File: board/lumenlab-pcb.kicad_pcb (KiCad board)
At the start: 2 copper layers, 74 parts, among them J1 2.1mm Barrel Jack, J2 01x04, J3 01x06, J4 JTAG, SW1 SW_SPST, U1 MP2338, U2 AP7361C-33E, U3 SN74AHCT1G125, U4 SN74HC14DR, U5 ESP32-WROOM-32E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

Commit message: Separate pcb layout into separate modules
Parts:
- moved J4 442.1 mm to (-168.3, 343.3)
- moved C23 397.5 mm to (433.7, 279.1)
- moved R22 397.5 mm to (432.9, 285.0)
- moved RV1 381.6 mm to (455.4, 352.0)
- moved C5 374.8 mm to (253.0, -186.6)
- moved C6 374.8 mm to (258.0, -186.6)
- moved R4 374.8 mm to (247.0, -188.1)
- moved R8 374.8 mm to (247.0, -184.6)
- moved R21 363.5 mm to (337.1, 342.0)
- moved U1 352.9 mm to (212.2, -190.2)
- moved R9 346.3 mm to (453.0, 285.0)
- moved U7 343.1 mm to (450.0, 150.0)
- moved C7 336.2 mm to (368.6, -148.6)
- moved C8 336.2 mm to (373.8, -155.2)
- moved U2 336.2 mm to (342.9, -146.0)
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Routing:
- net +12V: track 0.63 -> 0.09 mm
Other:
- copper layers 2 -> 4

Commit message: Redesign the OLED user interface, implement USB programming
Due to testing with a hand soldered prototype, the original design of
using a five-way navigation tactile switch for the display navigation
was removed due to the button's fragility. A push button can be
registered as a push, down, and right command. The display will be
navigated using the PS3 controller, as that was already accessible.
USB-C periphials were added for more universal firmware updates, instead
of requiring the use of the ESP-Prog.
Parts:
- removed C24: 0.1uF, Capacitor_SMD:C_0603_1608Metric_Pad1.08x0.95mm_HandSolder
- removed R18: 100, Resistor_SMD:R_0603_1608Metric_Pad0.98x0.95mm_HandSolder
- removed R19, R22: 47K, Resistor_SMD:R_0603_1608Metric_Pad0.98x0.95mm_HandSolder
- removed S1: JS5208, 2_Vendor_NavSwitch:504-nav-switch
- removed U4: SN74HC14DR, 2_Vendor_SN74HC14N:sn74hc14dr
- added D2: ESD122DMYR, 2_Vendor_ESD122:DIO_ESD122DMYR, F.Cu at (-124.1, 136.7)
- added J5: USB_C_Receptacle_USB2.0_16P, Connector_USB:USB_C_Receptacle_JAE_DX07S016JA1R1500, F.Cu at (-154.7, 132.7)
- added U8: CP2102N-Axx-xQFN24, Package_DFN_QFN:QFN-24-1EP_4x4mm_P0.5mm_EP2.15x2.15mm, F.Cu at (-157.5, 140.5)
- C19, C20: value 0.1uF -> 100nF
- R12, R9: value 47K -> 5.1K
- R13, R14: value 100 -> 1K
- R15: value 100 -> 10K
- R16: value 47K -> 22
- R17: value 100 -> 22
- SW1: moved to B.Cu
- moved R16 634.2 mm to (-128.1, 136.5)
- moved R17 597.7 mm to (-128.1, 142.0)
- moved SW1 302.8 mm to (251.9, 100.0), turned to 180 degrees
- moved J1 298.2 mm to (252.9, 60.0), turned to 90 degrees
- moved C2 287.5 mm to (213.5, 90.0)
- moved C5 287.5 mm to (179.6, 91.4)
- moved C6 287.5 mm to (184.6, 91.4)
- moved R4 287.5 mm to (173.6, 89.9)
- moved R8 287.5 mm to (173.6, 93.4)
- moved U1 287.5 mm to (138.8, 87.8)
- moved C1 273.6 mm to (142.9, 101.5)
- moved C10 273.6 mm to (185.3, 105.3)
- moved C3 273.6 mm to (193.5, 105.5)
- moved C9 273.6 mm to (186.3, 114.9)
- moved L1 273.6 mm to (176.3, 110.5)
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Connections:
- C15 pad 1: /DEBOUNCE_UP -> +3.3V
- C18 pad 1: GND -> +3.3V
- C18 pad 2: +3.3V -> GND
- C19 pad 1: /DEBOUNCE_DOWN -> Net-(U8-~{DTR})
- C19 pad 2: GND -> /ESP32_GPIO0
- C20 pad 1: /DEBOUNCE_LEFT -> Net-(U8-~{RTS})
- C20 pad 2: GND -> /ESP32_EN
- C23 pad 1: /DEBOUNCE_RIGHT -> Net-(U8-~{RST})
- R10 pad 2: Net-(U5-EN) -> /ESP32_EN
- R11 pad 2: Net-(U5-IO0) -> /ESP32_GPIO0
- R12 pad 1: +3.3V -> Net-(J5-CC2)
- R12 pad 2: /DEBOUNCE_DOWN -> GND
- R13 pad 1: /ESP32_GPIO32 -> Net-(U8-RXD)
- R13 pad 2: Net-(U4-1Y) -> /ESP32_TX
- R14 pad 1: /ESP32_GPIO27 -> Net-(U8-TXD)
- R14 pad 2: Net-(U4-5Y) -> /ESP32_RX
- R15 pad 1: /ESP32_GPIO33 -> Net-(U8-~{RST})
- R15 pad 2: Net-(U4-2Y) -> +3.3V
- R16 pad 1: +3.3V -> Net-(D2-Pad2)
- R16 pad 2: /DEBOUNCE_LEFT -> /DATA-
- R17 pad 2: /ESP32_GPIO35 -> /DATA+
- R9 pad 1: +3.3V -> Net-(J5-CC1)
- R9 pad 2: /DEBOUNCE_UP -> GND
- TP1 pad 1: Net-(U5-EN) -> /ESP32_EN
- TP2 pad 1: Net-(U5-IO0) -> /ESP32_GPIO0
- U5 pad 12: /ESP32_GPIO27 -> unconnected-(U5-IO27-Pad12)
- U5 pad 25: Net-(U5-IO0) -> /ESP32_GPIO0
- U5 pad 3: Net-(U5-EN) -> /ESP32_EN
- U5 pad 31: /ESP32_GPIO19 -> unconnected-(U5-IO19-Pad31)
- U5 pad 34: unconnected-(U5-RXD0/IO3-Pad34) -> /ESP32_RX
- U5 pad 35: unconnected-(U5-TXD0/IO1-Pad35) -> /ESP32_TX
- U5 pad 7: /ESP32_GPIO35 -> unconnected-(U5-IO35-Pad7)
- U5 pad 8: /ESP32_GPIO32 -> unconnected-(U5-IO32-Pad8)
- U5 pad 9: /ESP32_GPIO33 -> unconnected-(U5-IO33-Pad9)
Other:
- board outline added: 195 x 111 mm

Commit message: Replace LED strip bare THT pads with JST 3.96mm. Replace decoupling THT cap for SMD
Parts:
- removed R20: 10, Resistor_SMD:R_0603_1608Metric_Pad0.98x0.95mm_HandSolder
- removed R21: 1K, Resistor_SMD:R_0603_1608Metric_Pad0.98x0.95mm_HandSolder
- removed U8: CP2102N-Axx-xQFN24, Package_DFN_QFN:QFN-24-1EP_4x4mm_P0.5mm_EP2.15x2.15mm
- added R18: 22, Resistor_SMD:R_0603_1608Metric_Pad0.98x0.95mm_HandSolder, F.Cu at (34.1, 322.5)
- added R19: 22, Resistor_SMD:R_0603_1608Metric_Pad0.98x0.95mm_HandSolder, F.Cu at (34.1, 325.0)
- added U4: SSD1306, 2_Custom_SSD1306:SSD1306_OLED_MODULE, F.Cu at (18.1, 335.4)
- C13: footprint 2_Vendor_16SEPF:CAPPRD500W60D1000H1300 -> 2_Vendor_EMZS250ARA102:CAP_JA0_NIP
- C16: value 0.1uF -> 1000uF; footprint Capacitor_SMD:C_0603_1608Metric_Pad1.08x0.95mm_HandSolder -> 2_Vendor_EMZS250ARA102:CAP_JA0_NIP
- C17: value 1000uF -> 0.1uF; footprint 2_Vendor_16SEPF:CAPPRD500W60D1000H1300 -> Capacitor_SMD:C_0603_1608Metric_Pad1.08x0.95mm_HandSolder
- C19: value 100nF -> 0.1uF
- C20: value 100nF -> 250uF; footprint Capacitor_SMD:C_0603_1608Metric_Pad1.08x0.95mm_HandSolder -> 2_Vendor_10TZV220M6:CAP_J-V_6P3X8_RUB-M
- C21: value 250uF -> 0.05uF; footprint 2_Vendor_10TZV220M6:CAP_J-V_6P3X8_RUB-M -> Capacitor_SMD:C_1206_3216Metric_Pad1.33x1.80mm_HandSolder
- C22: value 0.05uF -> 0.1uF; footprint Capacitor_SMD:C_1206_3216Metric_Pad1.33x1.80mm_HandSolder -> Capacitor_SMD:C_0603_1608Metric_Pad1.08x0.95mm_HandSolder
- J2: value 01x04 -> 01x06; footprint Connector_Wire:SolderWire-0.75sqmm_1x04_P7mm_D1.25mm_OD3.5mm -> Connector_JST:JST_VH_B6PS-VH_1x06_P3.96mm_Horizontal
- J3: value 01x06 -> 01x04; footprint Connector_Wire:SolderWire-0.75sqmm_1x06_P7mm_D1.25mm_OD3.5mm -> Connector_JST:JST_VH_B4PS-VH_1x04_P3.96mm_Horizontal
- R11, R15: value 10K -> 1K
- R12, R9: value 5.1K -> 10K
- R14: value 1K -> 10
- R16, R17: value 22 -> 5.1K
- R5: value 10K -> 330
- R6: value 330 -> 10K
- U5: value ESP32-WROOM-32E -> LM386MX; footprint RF_Module:ESP32-WROOM-32E -> digikey-footprints:SOIC-8_W3.9mm
- U6: value LM386MX -> ESP32-WROOM-32E; footprint digikey-footprints:SOIC-8_W3.9mm -> RF_Module:ESP32-WROOM-32E
- U7: value SSD1306 -> CP2102N-Axx-xQFN24; footprint 2_Custom_SSD1306:SSD1306_OLED_MODULE -> Package_DFN_QFN:QFN-24-1EP_4x4mm_P0.5mm_EP2.15x2.15mm
- moved H1 429.5 mm to (259.0, 51.0)
- moved F1 15.9 mm to (251.9, 67.8)
- moved C16 15.0 mm to (160.5, 362.0)
- moved D1 8.93 mm to (248.0, 60.0), turned to -90 degrees
- moved C13 7.16 mm to (139.0, 362.0)
- moved C14 7.00 mm to (185.0, 342.2)
- moved J2 6.46 mm to (154.1, 329.2)
- moved J1 6.13 mm to (259.0, 61.0)
- moved C17 6.12 mm to (176.1, 360.0)
- moved SW1 2.30 mm to (254.0, 99.0)
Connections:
- C15 pad 1: +3.3V -> +12V
- C17 pad 1: +12V -> +3.3V
- C19 pad 1: Net-(U8-~{DTR}) -> Net-(U7-~{RST})
- C19 pad 2: /ESP32_GPIO0 -> GND
- C20 pad 1: Net-(U8-~{RTS}) -> Net-(C20-Pad1)
- C20 pad 2: /ESP32_EN -> Net-(C20-Pad2)
- C21 pad 1: Net-(C21-Pad1) -> Net-(C20-Pad1)
- C22 pad 1: Net-(C21-Pad1) -> Net-(U7-~{RTS})
- C22 pad 2: Net-(C22-Pad2) -> /ESP32_EN
- C23 pad 1: Net-(U8-~{RST}) -> Net-(U7-~{DTR})
- C23 pad 2: GND -> /ESP32_GPIO0
- J2 pad 3: GND -> /LED_DIN
- J2 pad 4: GND -> /LED_DIN
- J3 pad 3: /LED_DIN -> GND
- J3 pad 4: /LED_DIN -> GND
- LS1 pad 1: Net-(C21-Pad2) -> Net-(C20-Pad2)
- R10 pad 2: /ESP32_EN -> /ESP32_GPIO0
- R11 pad 1: +3.3V -> Net-(U7-TXD)
- R11 pad 2: /ESP32_GPIO0 -> /ESP32_RX
- R12 pad 1: Net-(J5-CC2) -> Net-(U7-~{RST})
- R12 pad 2: GND -> +3.3V
- R13 pad 1: Net-(U8-RXD) -> Net-(U7-RXD)
- R14 pad 1: Net-(U8-TXD) -> GND
- R14 pad 2: /ESP32_RX -> Net-(C21-Pad2)
- R15 pad 1: Net-(U8-~{RST}) -> Net-(R15-Pad1)
- R15 pad 2: +3.3V -> /ESP32_GPIO34
- R16 pad 1: Net-(D2-Pad2) -> Net-(J5-CC1)
- R16 pad 2: /DATA- -> GND
- R17 pad 1: Net-(D2-Pad3) -> Net-(J5-CC2)
- R17 pad 2: /DATA+ -> GND
- R5 pad 1: /BUCK_PG -> Net-(U3-Y)
- R5 pad 2: +5V -> /LED_DIN
- R6 pad 1: Net-(U3-Y) -> /BUCK_PG
- R6 pad 2: /LED_DIN -> +5V
- R9 pad 1: Net-(J5-CC1) -> +3.3V
- R9 pad 2: GND -> /ESP32_EN
- RV2 pad 2: Net-(R21-Pad1) -> Net-(R15-Pad1)
- U5 pad 1: GND -> unconnected-(U5-Pad1)
- U5 pad 2: +3.3V -> GND
- U5 pad 3: /ESP32_EN -> /AMP_IN
- U5 pad 4: unconnected-(U5-SENSOR_VP-Pad4) -> GND
- U5 pad 5: unconnected-(U5-SENSOR_VN-Pad5) -> Net-(C20-Pad1)
- U5 pad 6: /ESP32_GPIO34 -> +5V
- U6 pad 1: unconnected-(U6-Pad1) -> GND
- U6 pad 2: GND -> +3.3V
- U6 pad 3: /AMP_IN -> /ESP32_EN
- U6 pad 4: GND -> unconnected-(U6-SENSOR_VP-Pad4)
- U6 pad 5: Net-(C21-Pad1) -> unconnected-(U6-SENSOR_VN-Pad5)
- U6 pad 6: +5V -> /ESP32_GPIO34
- U7 pad 1: GND -> unconnected-(U7-~{RI}/CLK-Pad1)
- U7 pad 2: +5V -> GND
- U7 pad 3: /ESP32_GPIO22 -> /DATA+
- U7 pad 4: /ESP32_GPIO21 -> /DATA-

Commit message: Place power delivery, power protection, and step-down regulator
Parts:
- moved C7 363.7 mm to (125.6, 122.0)
- moved C8 363.7 mm to (130.7, 115.3)
- moved H2 361.0 mm to (235.0, 137.0)
- moved U2 352.4 mm to (127.2, 132.7)
- moved C22 316.9 mm to (503.1, 154.0)
- moved U6 264.7 mm to (168.2, 75.6), turned to 0 degrees
- moved J3 241.9 mm to (227.2, 107.9), turned to 90 degrees
- moved R6 239.7 mm to (214.0, 129.0), turned to -90 degrees
- moved C21 235.2 mm to (483.6, 268.0)
- moved R5 222.4 mm to (351.9, -46.0)
- moved LS1 160.0 mm to (383.0, 345.4)
- moved U1 83.0 mm to (213.0, 124.8), turned to 180 degrees
- moved C1 72.9 mm to (209.2, 131.8), turned to 180 degrees
- moved R2 72.4 mm to (212.0, 129.0), turned to -90 degrees
- moved R3 68.8 mm to (209.1, 128.8), turned to 180 degrees
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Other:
- board size 195 x 111 mm -> 148.5 x 80 mm

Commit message: Add LDO, signal JST connector, OLED display, and UI potentiometers
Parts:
- added TP6: LED_SIG, TestPoint:TestPoint_THTPad_D2.0mm_Drill1.0mm, F.Cu at (-158.0, 255.0)
- RV1, RV2: footprint Potentiometer_THT:Potentiometer_Piher_T-16L_Single_Vertical_Hole -> 2_Custom_Potentiometer:Potentiometer; moved to F.Cu
- TP1: value TestPoint -> 12V
- TP2: value TestPoint -> EN
- TP3: value TestPoint -> IO0
- TP4: value TestPoint -> 3.3V
- TP5: value TestPoint -> 5V
- U4: moved to B.Cu
- moved TP1 678.6 mm to (-158.0, 223.0)
- moved TP2 601.0 mm to (-158.0, 232.0)
- moved RV1 403.7 mm to (127.5, 116.5), turned to -90 degrees
- moved R12 375.0 mm to (176.5, 72.7), turned to -90 degrees
- moved R9 372.4 mm to (138.9, 85.0)
- moved C22 370.2 mm to (139.0, 87.5)
- moved C19 364.0 mm to (179.4, 71.8)
- moved C11 360.7 mm to (133.4, 80.0)
- moved C12 355.1 mm to (138.9, 82.0)
- moved J5 354.6 mm to (196.3, 82.5), turned to 90 degrees
- moved R15 346.6 mm to (132.5, 114.2)
- moved TP4 339.8 mm to (139.0, 79.0)
- moved C15 337.5 mm to (187.0, 119.1), turned to 90 degrees
- moved H3 327.5 mm to (103.0, 73.0)
- moved R13 327.1 mm to (165.1, 81.5), turned to 180 degrees
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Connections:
- TP1 pad 1: /ESP32_EN -> +12V
- TP2 pad 1: /ESP32_GPIO0 -> /ESP32_EN
- TP3 pad 1: +3.3V -> /ESP32_GPIO0
- TP4 pad 1: +5V -> +3.3V
- TP5 pad 1: /LED_DIN -> +5V
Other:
- board size 148.5 x 80 mm -> 100 x 65 mm
- copper layers 4 -> 2

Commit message: Place remaining components, audo, JTAG, filters
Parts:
- added C24: 0.1uF, Capacitor_SMD:C_0603_1608Metric_Pad1.08x0.95mm_HandSolder, F.Cu at (164.1, 95.5)
- added R20: 4.7K, Resistor_SMD:R_0603_1608Metric_Pad0.98x0.95mm_HandSolder, F.Cu at (164.1, 84.5)
- added R21: 4.7K, Resistor_SMD:R_0603_1608Metric_Pad0.98x0.95mm_HandSolder, F.Cu at (164.1, 80.0)
- R7: value 100 -> 33
- moved J4 402.2 mm to (152.2, 100.2)
- moved C21 357.8 mm to (120.0, 106.8)
- moved R14 357.8 mm to (120.0, 109.0)
- moved TP1 356.2 mm to (184.9, 126.6)
- moved C20 353.1 mm to (119.0, 121.8), turned to -90 degrees
- moved TP3 352.8 mm to (165.5, 99.2)
- moved U5 340.9 mm to (118.3, 101.3), turned to 90 degrees
- moved LS1 329.5 mm to (119.0, 129.9)
- moved TP2 329.4 mm to (143.5, 99.2)
- moved TP5 316.3 mm to (110.5, 81.0)
- moved TP6 308.6 mm to (116.5, 114.0)
- moved R5 281.5 mm to (120.2, 114.0), turned to 180 degrees
- moved R7 264.8 mm to (164.1, 89.0), turned to 180 degrees
- moved C4 261.2 mm to (164.1, 94.0), turned to 180 degrees
- moved U3 236.1 mm to (164.6, 91.5), turned to 180 degrees
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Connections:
- U4 pad 3: /ESP32_GPIO22 -> Net-(U4-SCL)
- U4 pad 4: /ESP32_GPIO21 -> Net-(U4-SDA)
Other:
- outline, holes or cut-outs redrawn

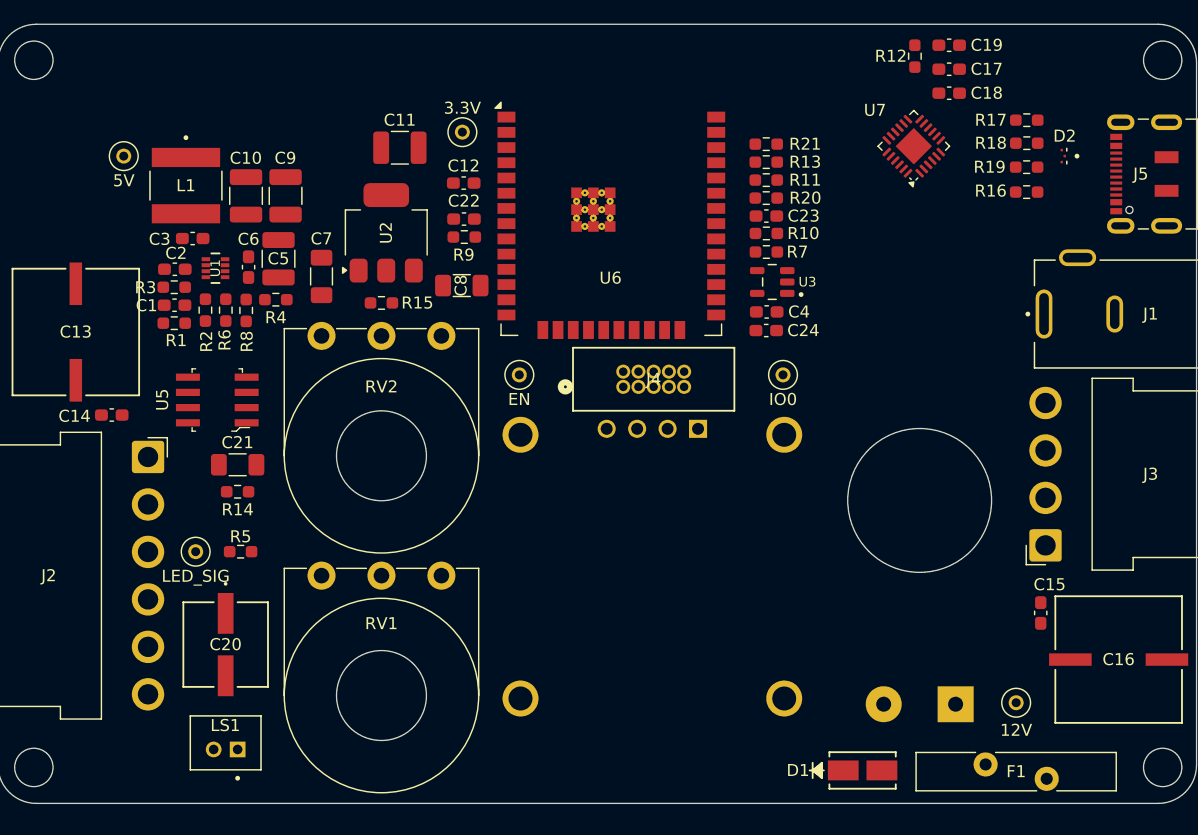
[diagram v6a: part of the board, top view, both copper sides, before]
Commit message: Route traces, tune differential pair
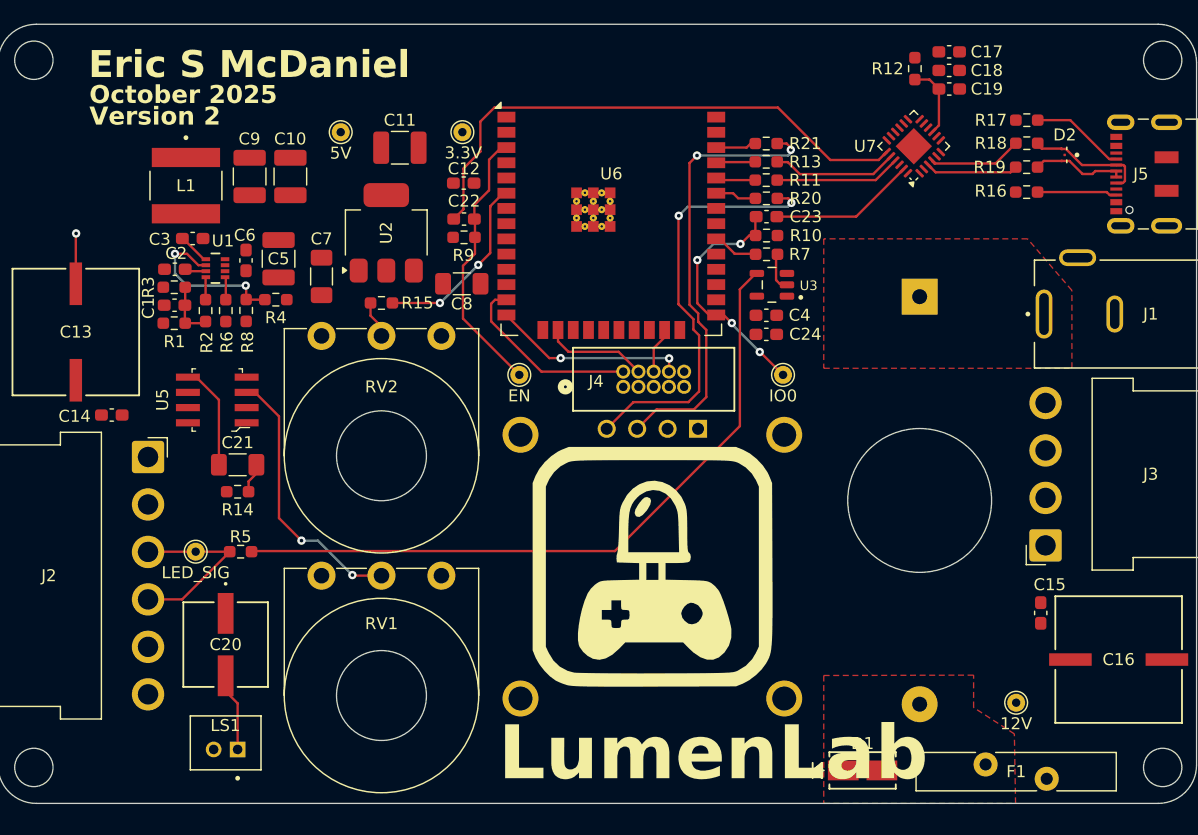
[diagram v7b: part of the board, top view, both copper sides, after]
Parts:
- added G***: LOGO, LOGO, F.Cu at (154.6, 115.2)
- TP1, TP2, TP3, TP4, TP5, TP6: footprint TestPoint:TestPoint_THTPad_D2.0mm_Drill1.0mm -> TestPoint:TestPoint_THTPad_D1.5mm_Drill0.7mm
- moved TP5 18.2 mm to (128.6, 79.0)
- moved C10 4.04 mm to (124.4, 82.7)
- moved C19 3.65 mm to (179.4, 75.4)
- moved C9 3.41 mm to (121.0, 82.7)
- moved C18 1.90 mm to (179.4, 73.8)
- moved C17 1.45 mm to (179.4, 72.3)
- moved R12 1.04 mm to (176.5, 73.7), turned to 90 degrees
- moved C6 0.60 mm to (120.7, 89.7)
- moved C24 0.32 mm to (164.1, 95.9)
- moved C4 0.28 mm to (164.1, 94.3)
- moved U3 0.24 mm to (164.6, 91.7)
- moved R7 0.19 mm to (164.1, 89.2)
- moved R10 0.18 mm to (164.1, 87.6)
- moved C8 0.15 mm to (138.7, 91.7)
- moved D2 0.10 mm to (188.9, 80.9)
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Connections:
- net Net-(D2-Pad2) renamed /USB_D-
- net Net-(D2-Pad3) renamed /USB_D+
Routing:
- net Net-(U3-Y): track 0.00 -> 58.5 mm
- net Net-(U7-~{RTS}): track 0.00 -> 45.8 mm
- net Net-(U4-SCL): track 0.00 -> 37.5 mm, vias 0 -> 2
- net Net-(U4-SDA): track 0.00 -> 35.6 mm, vias 0 -> 2
- net /ESP32_EN: track 0.00 -> 22.9 mm
- net /AMP_IN: track 0.00 -> 22.6 mm, vias 0 -> 2
- net /ESP32_GPIO0: track 0.00 -> 20.9 mm, vias 0 -> 4
- net /ESP32_GPIO12: track 0.00 -> 16.2 mm, vias 0 -> 2
- net /ESP32_GPIO14: track 0.00 -> 15.6 mm
- net /ESP32_GPIO34: track 0.00 -> 15.6 mm, vias 0 -> 2
- net /LED_DIN: track 0.00 -> 15.3 mm
- net /BUCK_EN: track 0.00 -> 13.7 mm, vias 0 -> 2
- net Net-(U7-~{DTR}): track 0.00 -> 12.2 mm
- net Net-(U7-RXD): track 0.00 -> 10.5 mm
- net Net-(U7-TXD): track 0.00 -> 10.5 mm
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- added copper zone on F.Cu, net /FUSE
- added copper zone on F.Cu, net Net-(SW1-A)
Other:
- board text added: "Eric S McDaniel"
- board text added: "LumenLab"
- board text added: "October 2025"
- board text added: "Version 2"
